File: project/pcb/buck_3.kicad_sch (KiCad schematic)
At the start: 17 parts, among them Q2 2N3904, U4 SN74HCT00N, U5 LM393P, U6 INA180A1IDBVR

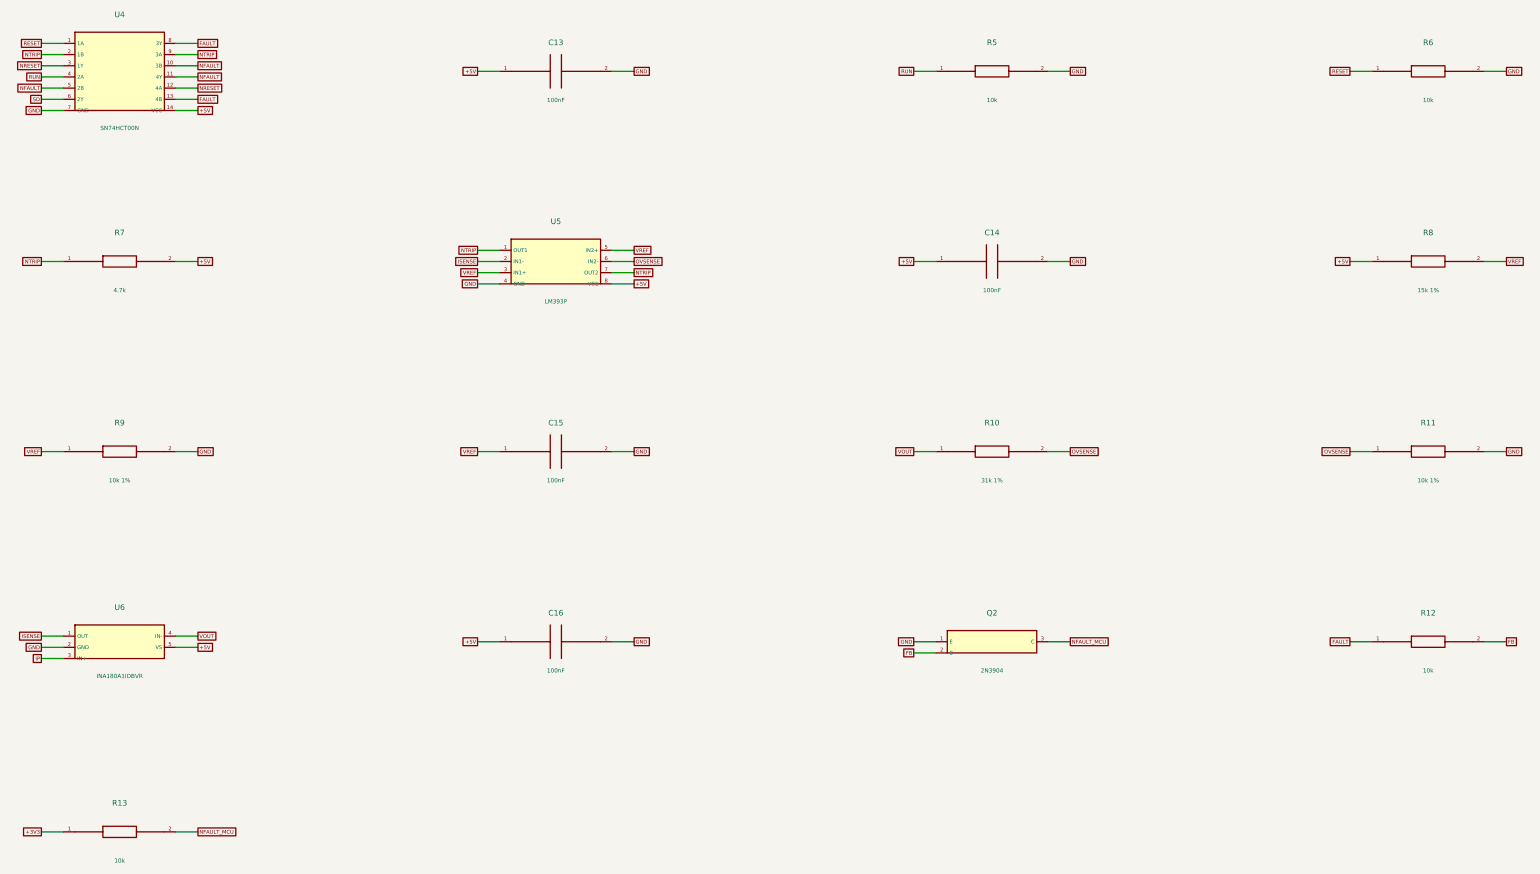
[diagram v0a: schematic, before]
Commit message: Preserve Buck PCB design and add validated JLCPCB quote package
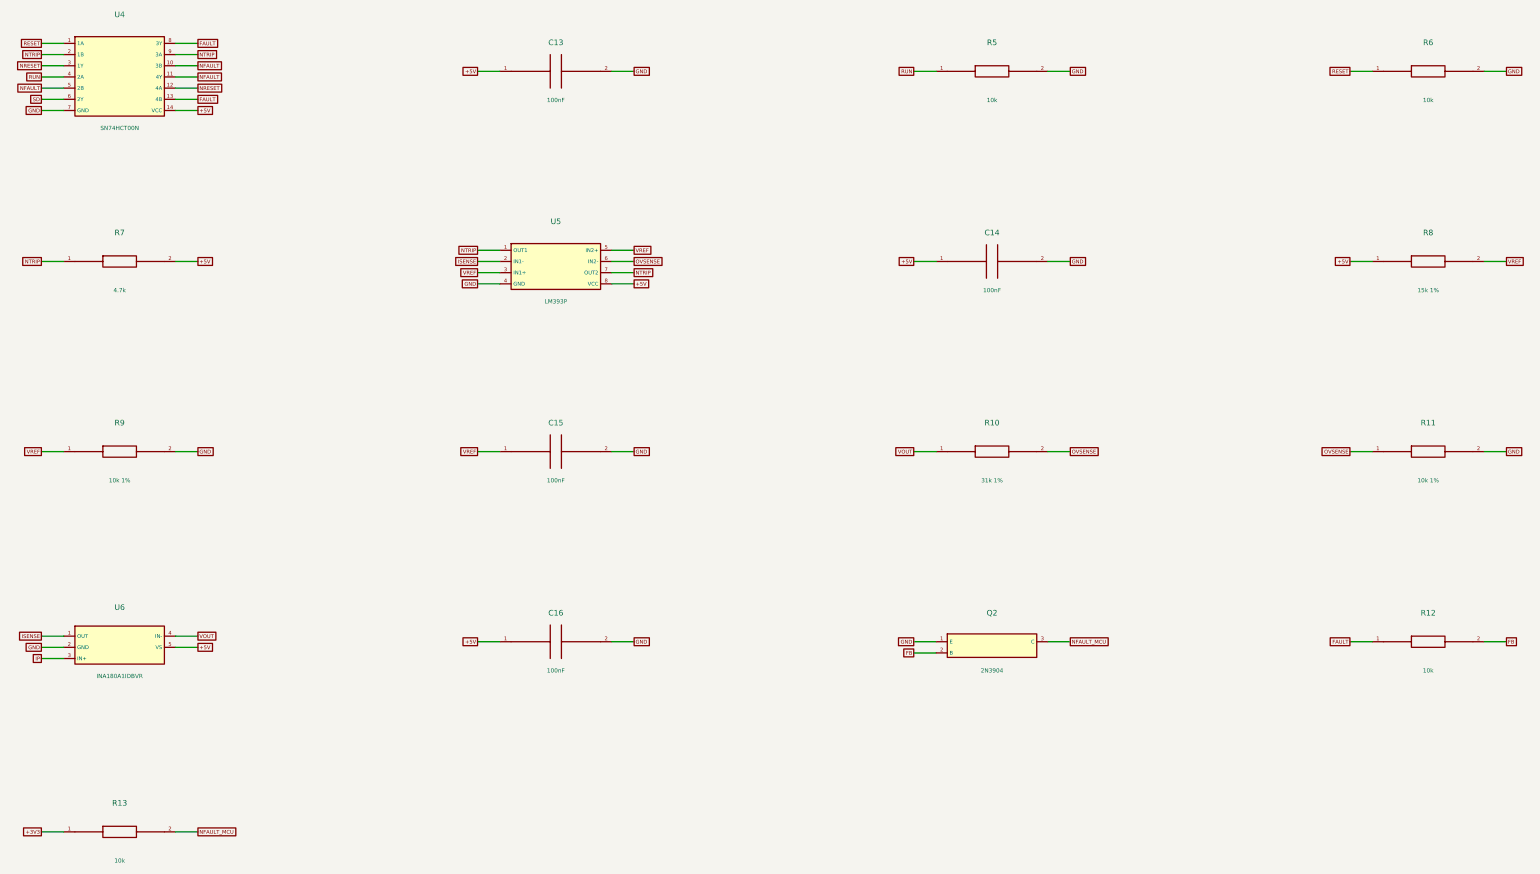
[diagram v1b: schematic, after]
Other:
- moved on the sheet: U4, U5
